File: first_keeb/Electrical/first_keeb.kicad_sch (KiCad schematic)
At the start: 5 parts, among them U1 Pico, U2 LM4040DBZ-3

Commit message: save the sch
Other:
- note added: "MCU Breakout (RP2040)"
- note removed: "MCU breakout"
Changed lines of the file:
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@@
     (stroke (width 0) (type default) (color 0 0 0 0))
   )
-  (text "MCU breakout" (at 13.335 16.51 0)
+  (text "MCU Breakout (RP2040)\n" (at 13.335 16.51 0)
     (effects (font (size 2 2)) (justify left bottom))
   )

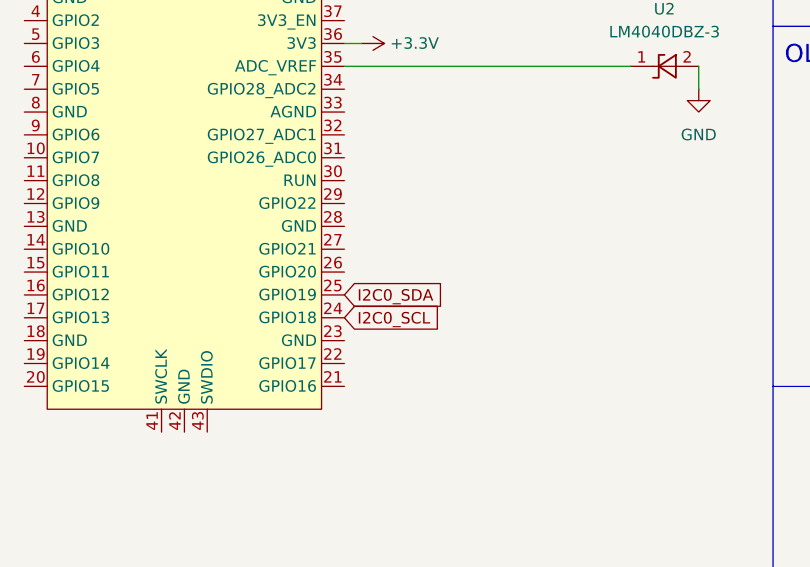
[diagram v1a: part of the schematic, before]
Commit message: fixes i2c and moves them to gpio that can only do i2c. Adds pico pinout picture
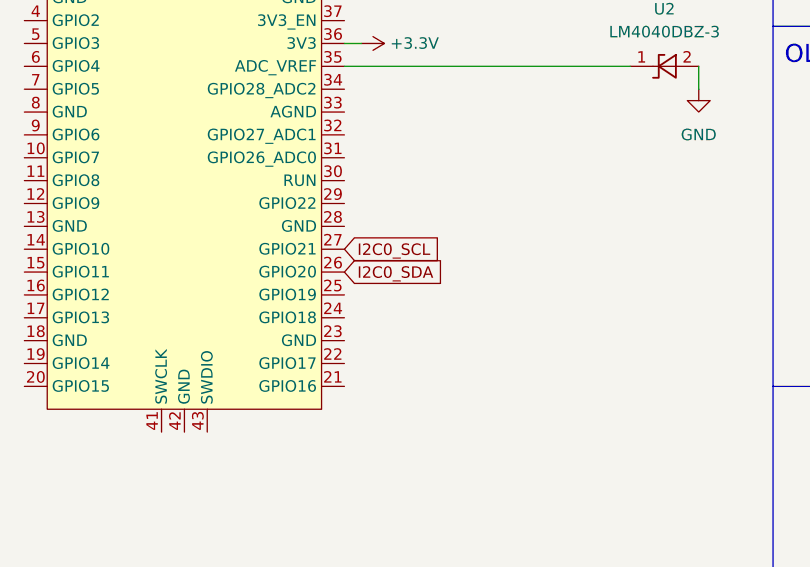
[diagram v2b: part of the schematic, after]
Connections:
- net I2C0_SCL: now also U1.27 (GPIO21); no longer U1.24 (GPIO18)
- net I2C0_SDA: now also U1.26 (GPIO20); no longer U1.25 (GPIO19)
